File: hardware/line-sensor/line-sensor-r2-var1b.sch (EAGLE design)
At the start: 154 parts, among them IC1 GP2S60, IC10 GP2S60, IC11 GP2S60, IC12 GP2S60, IC13 GP2S60, IC14 GP2S60, IC15 GP2S60, IC16 GP2S60, IC17 GP2S60, IC18 GP2S60, IC19 GP2S60, IC2 GP2S60, IC20 GP2S60, IC21 GP2S60, IC22 GP2S60, IC23 GP2S60, IC24 GP2S60, IC25 GP2S60, IC26 STM32L151VE, IC27 TI-LM5165YDRCR, IC28 TI-TPS62170, IC29 AD-REF196GSZ, IC3 GP2S60, IC30 AD-ADP124ARHZ, IC4 GP2S60, IC5 GP2S60, IC6 GP2S60, IC7 GP2S60, IC8 GP2S60, IC9 GP2S60, J1 MOLEX-502382-02XX, J2 MOLEX-502382-05XX, J3 MOLEX-53261-0771

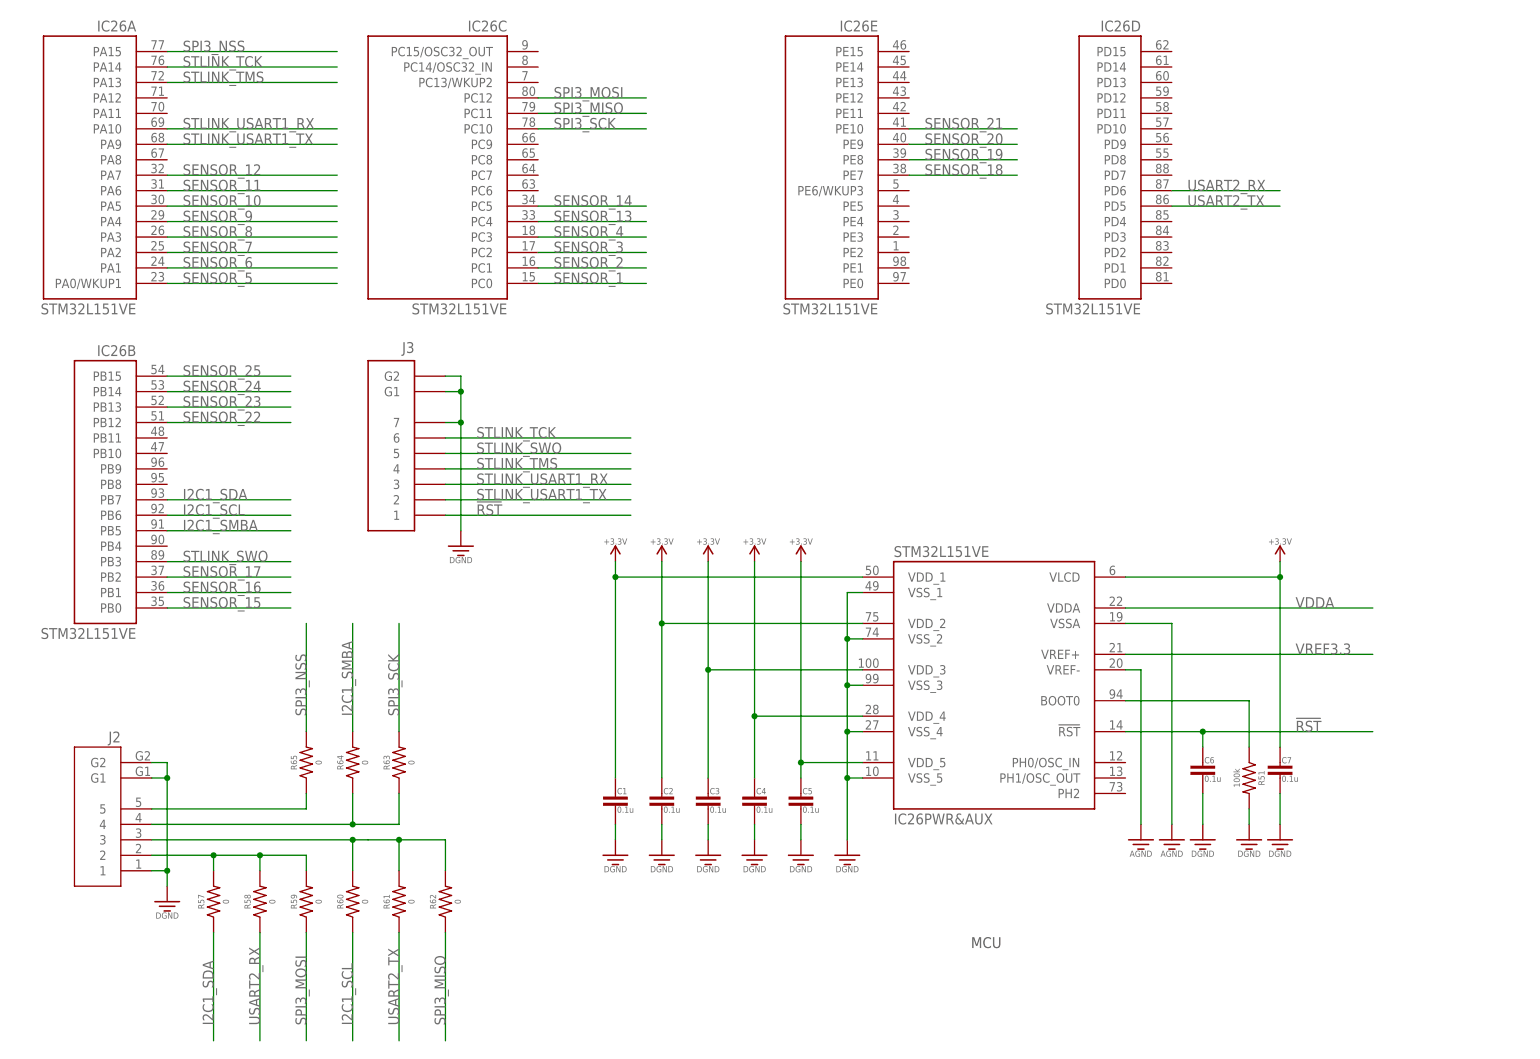
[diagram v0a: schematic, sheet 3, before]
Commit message: - starting to use TLA for proof of algorithms - fixed line sensor R2 VAR1B schematic a bit (needs a lot more work, after I pick resistor values and voltage ranges) - minor fixes in documentation - migrated deterministic os to latest STM32 package - fixed deterministic os example
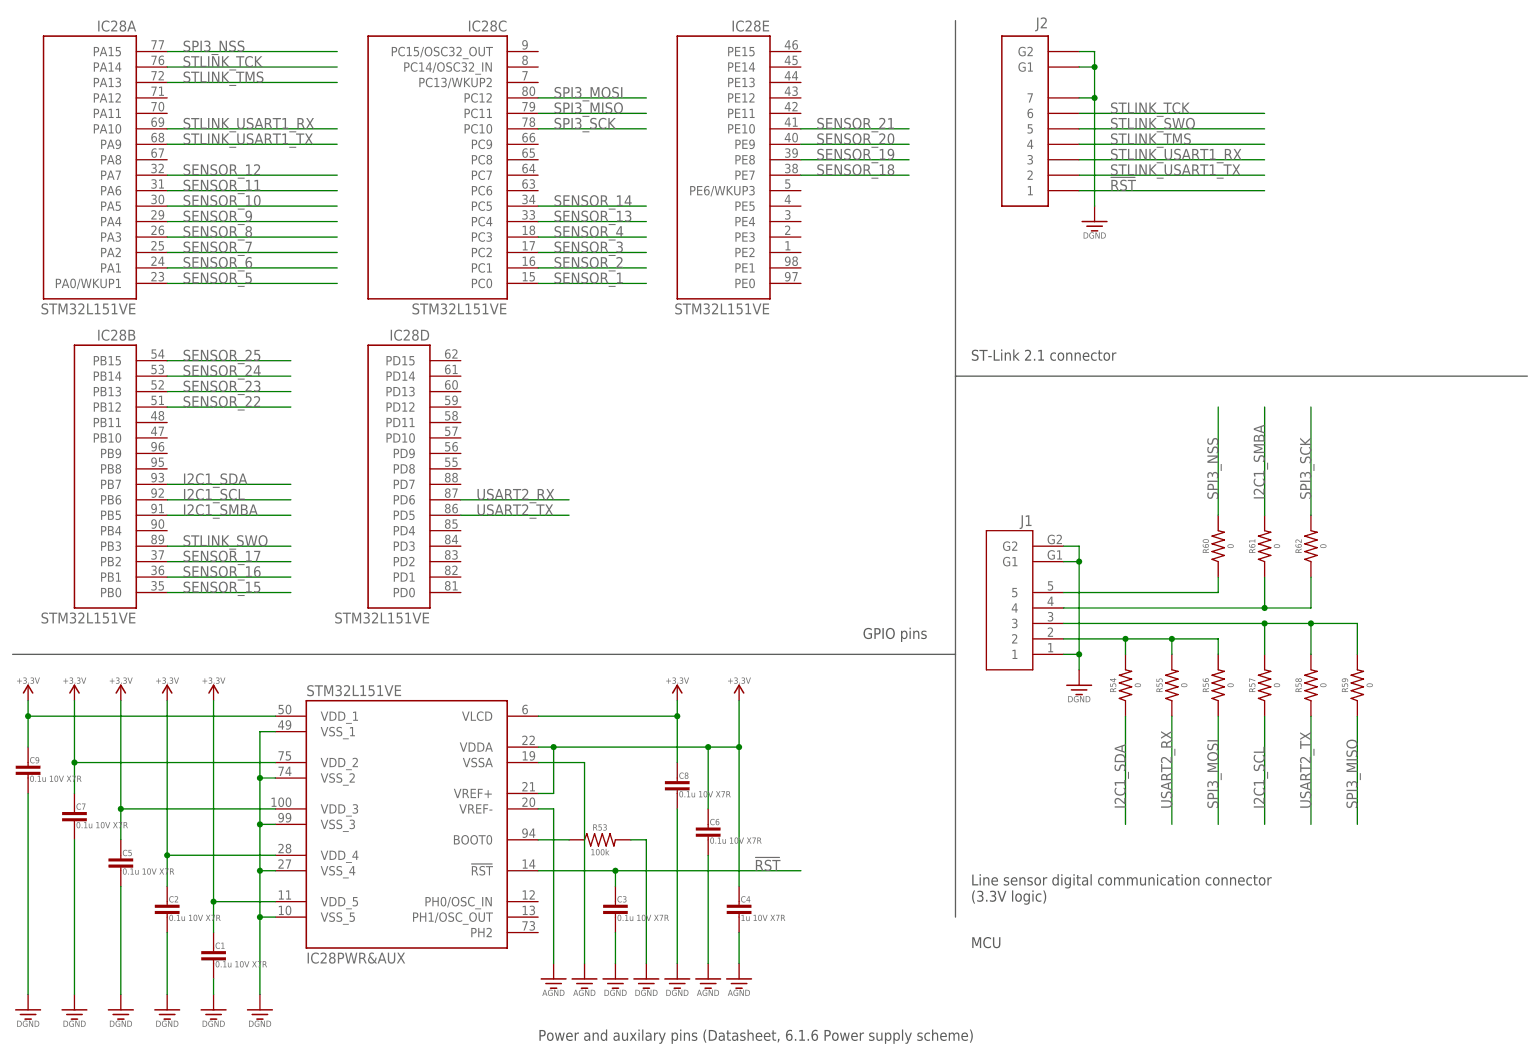
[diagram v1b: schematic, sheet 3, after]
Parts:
- removed C13: 22u 10V X7R, capacitors:CAPACITOR0805
- removed C14: 10u 50V, capacitors:CAPACITOR0603
- removed C15, C18: 1u 10V X7R, capacitors:CAPACITOR0805
- removed C16: 0.1u 50V, capacitors:CAPACITOR0603
- removed C17: 1u 10V Tant, capacitors:CAPACITOR_POLARIZED
- removed C19, C20: 0.1u 10V X7R, capacitors:CAPACITOR0603
- removed IC30: AD-ADP124ARHZ, voltage-source:AD-ADP124ARHZ
- removed L2: 150u 0.35A, inductors:ELL-6SH151M
- removed R65: 0, resistors:RESISTOR_0.1W
- removed SUPPLY1: +3.3V, voltage-ground:+3.3V
- added SUPPLY35: +VBAT, voltage-ground:+VBAT
- added SUPPLY36: +3.5V, voltage-ground:+3.5V
- C1, C2, C3, C5, C6, C7: value 0.1u -> 0.1u 10V X7R
- C10: value 33n 10V X7R -> 22u 10V X7S; device capacitors:CAPACITOR0603 -> passives:CAPACITOR0805
- C11: value 22u 10V X7S -> 33n 10V X7R; device capacitors:CAPACITOR0805 -> passives:CAPACITOR0603
- C12: value 4.7u -> 1u 50V X7R; device capacitors:CAPACITOR0805 -> passives:CAPACITOR1206
- C4: value 0.1u -> 1u 10V X7R
- C8: value 10u 50V X7R -> 0.1u 10V X7R; device capacitors:CAPACITOR0805 -> capacitors:CAPACITOR0603
- C9: value 1u 50V X7R -> 0.1u 10V X7R; device capacitors:CAPACITOR1206 -> capacitors:CAPACITOR0603
- IC26: value STM32L151VE -> GP2S60; device mcu:STM32L151VE -> sensors:GP2S60
- IC27: value TI-LM5165YDRCR -> GP2S60; device voltage-source:TI-LM5165YDRCR -> sensors:GP2S60
- IC28: value TI-TPS62170 -> STM32L151VE; device voltage-source:TI-TPS62170 -> mcu:STM32L151VE
- IC29: value AD-REF196GSZ -> LM5165YDRCR; device voltage-source:AD-REF196GSZ -> voltage-regulator:LM5165YDRCR
- J1: value MOLEX-502382-02XX -> MOLEX-502382-05XX; device connectors:MOLEX-502382-02XX -> connectors:MOLEX-502382-05XX
- J2: value MOLEX-502382-05XX -> MOLEX-53261-0771; device connectors:MOLEX-502382-05XX -> connectors:MOLEX-53261-0771
- J3: value MOLEX-53261-0771 -> MOLEX-502382-02XX; device connectors:MOLEX-53261-0771 -> connectors:MOLEX-502382-02XX
- L1: value 3.3u 2.63A -> 150u 0.86R 0.35A; device inductors:VLS3012HBX -> passives:INDUCTORPANASONIC-SERIES-H
- R1: value 1k -> 1k 1% 0.1W
- R10, R14, R18, R22, R26, R34, R38, R42, R6: value 1k -> 220k
- R11, R15, R19, R23, R27, R3, R31, R35, R39, R43, R7: value 220k -> 1k
- R2: value 1k -> 220k 1% 0.1W
- R51: value 100k -> 1k
- R52: value 121k 1% -> 220k
- R53: value 100k 1% -> 100k
- R54: value 0.5 1% -> 0
- R55: value 610k 1% -> 0
- R56: value 180k 1% -> 0
- R63: value 0 -> 121k 1%; device resistors:RESISTOR_0.1W -> passives:RESISTOR0603
- R64: value 0 -> 0.5 5%; device resistors:RESISTOR_0.1W -> passives:RESISTOR0603
- SUPPLY32, SUPPLY33, SUPPLY34: value +VBAT -> +3.3V; device voltage-ground:+VBAT -> voltage-ground:+3.3V
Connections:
- removed net IC27_SW: IC27.SW, L2.P$1
- removed net IC28_SW: IC28.SW, L1.P$1
- removed net N$10 (its old number): IC8.4, R14.1
- removed net N$13 (its old number): IC12.4, R22.1
- removed net N$33: IC27.RT, R52.1
- removed net N$34: C10.1, IC27.SS
- removed net N$36: C11.1, R54.2
- removed net N$38: IC28.PG, R53.1
- removed net N$39: IC28.FB, R55.1, R56.2
- removed net N$8 (its old number): IC4.4, R6.1
- removed net VDDA: C18.1, C20.1, IC26PWR&AUX.VDDA, IC30.VOUT_1, IC30.VOUT_2, IC30.VOUT_SENSE, R1.2, R10.2, R11.2, R12.2, R13.2, R14.2, R15.2, R16.2, R17.2, R18.2, R19.2, R2.2, R20.2, R21.2, R22.2, R23.2, R24.2, R25.2, R26.2, R27.2, R28.2, R29.2, R3.2, R30.2, R31.2, R32.2, R33.2, R34.2, R35.2, R36.2, R37.2, R38.2, R39.2, R4.2, R40.2, R41.2, R42.2, R43.2, R44.2, R45.2, R46.2, R47.2, R48.2, R49.2, R5.2, R50.2, R6.2, R7.2, R8.2, R9.2, SUPPLY1.VCC, SUPPLY10.VCC, SUPPLY11.VCC, SUPPLY12.VCC, SUPPLY13.VCC, SUPPLY14.VCC, SUPPLY15.VCC, SUPPLY16.VCC, SUPPLY17.VCC, SUPPLY18.VCC, SUPPLY19.VCC, SUPPLY2.VCC, SUPPLY20.VCC, SUPPLY21.VCC, SUPPLY22.VCC, SUPPLY23.VCC, SUPPLY24.VCC, SUPPLY25.VCC, SUPPLY3.VCC, SUPPLY4.VCC, SUPPLY5.VCC, SUPPLY6.VCC, SUPPLY7.VCC, SUPPLY8.VCC, SUPPLY9.VCC
- removed net VDDA3.5: C13.1, C15.1, IC28.VOS, IC30.EN, IC30.VIN_1, IC30.VIN_2, L1.P$2, R53.2, R55.2
- removed net VREF3.3: C17.POS, C19.1, IC26PWR&AUX.VREF+, IC29.OUT
- new net IC32_SW: IC29.SW, L1.P$1
- new net N$15: IC21.4, R39.1
- new net N$22: IC17.4, R31.1
- new net N$3: IC10.4, R19.1
- new net N$35: IC29.RT, R63.1
- new net N$40: C11.1, IC29.SS
- new net N$42: C10.1, R64.2
- new net N$5: IC12.4, R23.1
- new net N$7: IC14.4, R27.1
- net !RST: now also C3.1, IC28PWR&AUX.!RST!, J2.1; no longer C6.1, IC26PWR&AUX.!RST!, J3.1
- net BOOT0: now also IC28PWR&AUX.BOOT0, R53.1; no longer IC26PWR&AUX.BOOT0, R51.1
- net GND: now also IC26.2, IC26.3, IC27.2, IC27.3, IC28PWR&AUX.VREF-, IC28PWR&AUX.VSSA, IC28PWR&AUX.VSS_1, IC28PWR&AUX.VSS_2, IC28PWR&AUX.VSS_3, IC28PWR&AUX.VSS_4, IC28PWR&AUX.VSS_5, IC29.ILIM, IC29.PAD, J1.1, J2.7, J3.2, R53.2, R63.2; no longer C13.2, C14.2, C15.2, C16.2, C17.NEG, C18.2, C19.2, C20.2, IC26PWR&AUX.VREF-, IC26PWR&AUX.VSSA, IC26PWR&AUX.VSS_1, IC26PWR&AUX.VSS_2, IC26PWR&AUX.VSS_3, IC26PWR&AUX.VSS_4, IC26PWR&AUX.VSS_5, IC27.GND, IC27.ILIM, IC27.PAD, IC28.AGND, IC28.PAD, IC28.PGND, IC30.GND, IC30.PAD, J1.2, J2.1, J3.7, R51.2, R52.2, R56.1
- net I2C1_SCL: now also IC28B.PB6, R57.1; no longer IC26B.PB6, R60.1
- net I2C1_SDA: now also IC28B.PB7, R54.1; no longer IC26B.PB7, R57.1
- net I2C1_SMBA: now also IC28B.PB5, R61.2; no longer IC26B.PB5, R64.2
- net N$11: now also IC6.4, R11.1; no longer IC10.4, R18.1
- net N$12: now also R3.1; no longer R2.1
- net N$14: now also IC8.4, R15.1; no longer IC14.4, R26.1
- net N$16: now also IC22.4, R41.1; no longer IC17.4, R33.1
- net N$17: now also IC23.4, R43.1; no longer IC19.4, R37.1
- net N$18: now also IC24.4, R45.1; no longer IC21.4, R41.1
- net N$19: now also IC25.4, R47.1; no longer IC23.4, R45.1
- net N$20: now also IC26.4, R49.1; no longer IC24.4, R47.1
- net N$21: now also IC27.4, R51.1; no longer IC25.4, R49.1
- net N$23: now also R33.1; no longer R34.1
- net N$24: now also IC19.4, R35.1; no longer IC20.4, R38.1
- net N$25: now also IC20.4, R37.1; no longer IC22.4, R42.1
- net N$26: now also J1.2, R54.2, R55.2, R56.2; no longer J2.2, R57.2, R58.2, R59.2
- net N$27: now also J1.3, R57.2, R58.2, R59.2; no longer J2.3, R60.2, R61.2, R62.2
- net N$28: now also J1.4, R61.1, R62.1; no longer J2.4, R63.1, R64.1
- net N$29: now also J1.5, R60.1; no longer J2.5, R65.1
- net N$9: now also IC4.4, R7.1; no longer IC6.4, R10.1
- net SENSOR_1: now also IC28C.PC0, R2.1; no longer IC26C.PC0, R3.1
- net SENSOR_10: now also IC28A.PA5, IC5.1, R10.1; no longer IC26A.PA5, IC8.1, R16.1
- net SENSOR_11: now also IC28A.PA6, IC6.1, R12.1; no longer IC10.1, IC26A.PA6, R20.1
- net SENSOR_12: now also IC28A.PA7; no longer IC26A.PA7
- net SENSOR_13: now also IC28C.PC4, IC7.1, R14.1; no longer IC12.1, IC26C.PC4, R24.1
- net SENSOR_14: now also IC28C.PC5, IC8.1, R16.1; no longer IC14.1, IC26C.PC5, R28.1
- net SENSOR_15: now also IC21.1, IC28B.PB0, R40.1; no longer IC15.1, IC26B.PB0, R31.1
- net SENSOR_16: now also IC22.1, IC28B.PB1, R42.1; no longer IC17.1, IC26B.PB1, R35.1
- net SENSOR_17: now also IC23.1, IC28B.PB2, R44.1; no longer IC19.1, IC26B.PB2, R39.1
- net SENSOR_18: now also IC24.1, IC28E.PE7, R46.1; no longer IC21.1, IC26E.PE7, R43.1
- net SENSOR_19: now also IC25.1, IC28E.PE8, R48.1; no longer IC23.1, IC26E.PE8, R46.1
- net SENSOR_2: now also IC28C.PC1, IC9.1, R18.1; no longer IC26C.PC1, IC3.1, R7.1
- net SENSOR_20: now also IC26.1, IC28E.PE9, R50.1; no longer IC24.1, IC26E.PE9, R48.1
- net SENSOR_21: now also IC27.1, IC28E.PE10, R52.1; no longer IC25.1, IC26E.PE10, R50.1
- net SENSOR_22: now also IC17.1, IC28B.PB12; no longer IC16.1, IC26B.PB12
- net SENSOR_23: now also IC28B.PB13, R34.1; no longer IC26B.PB13, R36.1
- net SENSOR_24: now also IC19.1, IC28B.PB14, R36.1; no longer IC20.1, IC26B.PB14, R40.1
- net SENSOR_25: now also IC20.1, IC28B.PB15, R38.1; no longer IC22.1, IC26B.PB15, R44.1
- net SENSOR_3: now also IC10.1, IC28C.PC2, R20.1; no longer IC26C.PC2, IC5.1, R11.1
- net SENSOR_4: now also IC11.1, IC28C.PC3, R22.1; no longer IC26C.PC3, IC7.1, R15.1
- net SENSOR_5: now also IC12.1, IC28A.PA0/WKUP1, R24.1; no longer IC26A.PA0/WKUP1, IC9.1, R19.1
- net SENSOR_6: now also IC13.1, IC28A.PA1, R26.1; no longer IC11.1, IC26A.PA1, R23.1
- net SENSOR_7: now also IC14.1, IC28A.PA2, R28.1; no longer IC13.1, IC26A.PA2, R27.1
- net SENSOR_8: now also IC28A.PA3, IC3.1, R6.1; no longer IC26A.PA3, IC4.1, R8.1
- net SENSOR_9: now also IC28A.PA4, IC4.1, R8.1; no longer IC26A.PA4, IC6.1, R12.1
- net SPI3_MISO: now also IC28C.PC11, R59.1; no longer IC26C.PC11, R62.1
- net SPI3_MOSI: now also IC28C.PC12, R56.1; no longer IC26C.PC12, R59.1
- net SPI3_NSS: now also IC28A.PA15, R60.2; no longer IC26A.PA15, R65.2
- net SPI3_SCK: now also IC28C.PC10, R62.2; no longer IC26C.PC10, R63.2
- net STLINK_SWO: now also IC28B.PB3, J2.5; no longer IC26B.PB3, J3.5
- net STLINK_TCK: now also IC28A.PA14, J2.6; no longer IC26A.PA14, J3.6
- net STLINK_TMS: now also IC28A.PA13, J2.4; no longer IC26A.PA13, J3.4
- net STLINK_USART1_RX: now also IC28A.PA10, J2.3; no longer IC26A.PA10, J3.3
- net STLINK_USART1_TX: now also IC28A.PA9, J2.2; no longer IC26A.PA9, J3.2
- net USART2_RX: now also IC28D.PD6, R55.1; no longer IC26D.PD6, R58.1
- net USART2_TX: now also IC28D.PD5, R58.1; no longer IC26D.PD5, R61.1
- net VBAT: now also C12.1, IC29.EN, IC29.VIN, J3.1, SUPPLY35.VCC; no longer C14.1, C16.1, C8.1, C9.1, IC27.EN, IC27.VIN, IC28.EN, IC28.VIN, IC29.!SLEEP, IC29.VS, J1.1, SUPPLY32.VCC, SUPPLY33.VCC, SUPPLY34.VCC
- net VDD: now also C6.1, C8.1, C9.1, IC28PWR&AUX.VDDA, IC28PWR&AUX.VDD_1, IC28PWR&AUX.VDD_2, IC28PWR&AUX.VDD_3, IC28PWR&AUX.VDD_4, IC28PWR&AUX.VDD_5, IC28PWR&AUX.VLCD, IC28PWR&AUX.VREF+, IC29.VOUT, L1.P$2, R1.2, R10.2, R11.2, R12.2, R13.2, R14.2, R15.2, R16.2, R17.2, R18.2, R19.2, R2.2, R20.2, R21.2, R22.2, R23.2, R24.2, R25.2, R26.2, R27.2, R28.2, R29.2, R3.2, R30.2, R31.2, R32.2, R33.2, R34.2, R35.2, R36.2, R37.2, R38.2, R39.2, R4.2, R40.2, R41.2, R42.2, R43.2, R44.2, R45.2, R46.2, R47.2, R48.2, R49.2, R5.2, R50.2, R51.2, R52.2, R6.2, R64.1, R7.2, R8.2, R9.2, SUPPLY10.VCC, SUPPLY11.VCC, SUPPLY12.VCC, SUPPLY13.VCC, SUPPLY14.VCC, SUPPLY15.VCC, SUPPLY16.VCC, SUPPLY17.VCC, SUPPLY18.VCC, SUPPLY19.VCC, SUPPLY2.VCC, SUPPLY20.VCC, SUPPLY21.VCC, SUPPLY22.VCC, SUPPLY23.VCC, SUPPLY24.VCC, SUPPLY25.VCC, SUPPLY3.VCC, SUPPLY32.VCC, SUPPLY33.VCC, SUPPLY34.VCC, SUPPLY36.VCC, SUPPLY4.VCC, SUPPLY5.VCC, SUPPLY6.VCC, SUPPLY7.VCC, SUPPLY8.VCC, SUPPLY9.VCC; no longer C12.1, C3.1, IC26PWR&AUX.VDD_1, IC26PWR&AUX.VDD_2, IC26PWR&AUX.VDD_3, IC26PWR&AUX.VDD_4, IC26PWR&AUX.VDD_5, IC26PWR&AUX.VLCD, IC27.VOUT, L2.P$2, R54.1
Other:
- note added: "Edge IR lights to even out readings from all sensors"
- note added: "GPIO pins"
- note added: "Line sensor digital communication connector (3.3V logic)"
- note added: "MCU switching voltage supply (3.3V, 150mA)"
- note added: "Power and auxilary pins (Datasheet, 6.1.6 Power supply scheme)"
- note added: "ST-Link 2.1 connector"
- note added: "VBAT range: Vmin = 4 V Vmax = 14 V Imax = 150 mA (70 mA typical)"
- note removed: "ADC power supply ADC reference voltage Sensors power supply"
- note removed: "Battery"
- note removed: "MCU power supply"
- note removed: "R4/R5 are used to set output voltage R5 must be < 400k VDDA3.5 voltage range: min = 3.45743 (smaller R4, larger R5) max = 3.56588 (larger R4, smaller R5)"
- note removed: "VBAT range: min = 4V max = 14V"
- moved on the sheet: C1, C10, C11, C12, C2, C3, C4, C5, C6, C7, L1, R10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
